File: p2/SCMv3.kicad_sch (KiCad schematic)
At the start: 122 parts, among them IC1 40106, IC2 40106, IC3 TL082, J1 ISP, J1-OUT8 JACK-MONO-SWB, J2 Conn_01x02, J2-OUT7 JACK-MONO-SWB, J3 POWER, J3-OUT6 JACK-MONO-SWB, J4-OUT5 JACK-MONO-SWB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

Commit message: SCM v3 updates
*added missing trace for buttons
*moved trip pot
*flipped pots around
*removed C18 and 21
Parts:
- removed C18, C21: 0.1uF_0603_16V, 4ms_Capacitor:C_0603, symbol 4ms_Capacitor:0.1uF_0603_16V
- D10, D11: JLCPCB ID (none) -> C15759
- IC1, IC2: JLCPCB ID (none) -> C58834
- IC3: JLCPCB ID (none) -> C2652280
- Q1, Q2, Q3, Q4: footprint Package_TO_SOT_SMD:SOT-23 -> 4ms_Package_SOT:SOT23-3_PO132; Display (none) -> Si2318; JLCPCB ID (none) -> C14498
- U1: value ATmega328-A -> ATMEGA328-AU; Alt JLCPCB ID (none) -> C618731; JLCPCB ID (none) -> C14877
- VR1: Alt JLCPCB ID (none) -> C55509; JLCPCB ID (none) -> C58069
- VR2: Alt JLCPCB ID (none) -> C8614; JLCPCB ID (none) -> C122847
- Y1: JLCPCB ID (none) -> C90906
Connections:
- net GND: now also IC1.7 (VSS), IC2.7 (VSS)
- net at BMUTE1.5 (POLE-B), R18.2: now also BMUTE1.2 (POLE-A), R22.2
- net at BFAST1.2 (POLE-A), R7.2: now also BFAST1.5 (POLE-B), R5.2

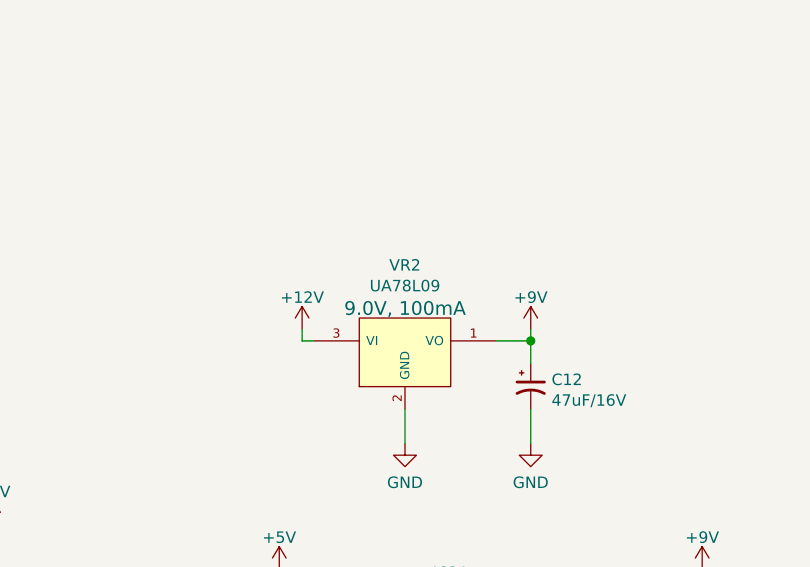
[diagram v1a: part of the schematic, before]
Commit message: replaced 9v reg with 8v reg
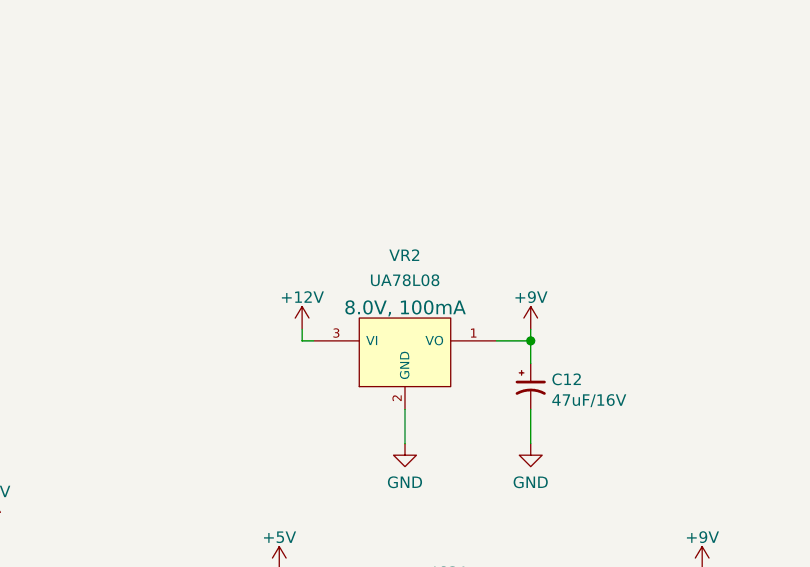
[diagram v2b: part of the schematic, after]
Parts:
- removed VR2: UA78L09, 4ms_Package_SOT:SOT89-3, symbol 4ms_Regulator:UA78L09
- added VR2: UA78L08, 4ms_Package_SOT:SOT89-3, symbol 4ms_Regulator:UA78L08
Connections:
- net +12V: now also VR2.3 (VI)
- net +9V: now also VR2.1 (VO)
- net GND: now also VR2.2 (GND)
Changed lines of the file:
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@@
     (pin "3")
   )
-  (symbol (lib_id "4ms_Regulator:UA78L09") (at 193.04 304.8 0) (unit 1)
+  (symbol (lib_id "4ms_Regulator:UA78L08") (at 193.04 304.8 0) (unit 1)
     (in_bom yes) (on_board yes) (fields_autoplaced)
-    (property "Reference" "VR2" (id 0) (at 193.04 295.1316 0))
-    (property "Value" "UA78L09" (id 1) (at 193.04 297.4303 0))
+    (property "Reference" "VR2" (id 0) (at 193.04 294.0628 0))
+    (property "Value" "UA78L08" (id 1) (at 193.04 296.8379 0))
     (property "Footprint" "4ms_Package_SOT:SOT89-3" (id 2) (at 204.47 317.5 0)
       (effects (font (size 1.27 1.27)) hide)
     )
-    (property "Datasheet" "https://www.ti.com/general/docs/suppproductinfo.tsp?distId=26&gotoUrl=http%3A%2F%2Fwww.ti.com%2Flit%2Fgpn%2Fua78l" (id 3) (at 193.04 304.8 0)
-      (effects (font (size 1.27 1.27)) hide)
-    )
-    (property "Specifications" "Vreg 9.0V, Iout>100mA, Vin>11.5V" (id 4) (at 190.5 312.674 0)
+    (property "Datasheet" "https://www.ti.com/lit/ds/symlink/ua78l.pdf?HQS=dis-mous-null-mousermode-dsf-pf-null-wwe&ts=1629320595639" (id 3) (at 193.04 304.8 0)
+      (effects (font (size 1.27 1.27)) hide)
+    )
+    (property "Specifications" "Vreg 8.0V, Iout>100mA, Vin>10.5V" (id 4) (at 190.5 312.674 0)
       (effects (font (size 1.27 1.27)) (justify left) hide)
     )
@@
       (effects (font (size 1.27 1.27)) (justify left) hide)
     )
-    (property "Part Number" "UA78L09ACPK" (id 6) (at 190.5 315.722 0)
-      (effects (font (size 1.27 1.27)) (justify left) hide)
-    )
-    (property "Display" "9.0V, 100mA" (id 7) (at 193.04 299.9335 0)
+    (property "Part Number" "UA78L08ACPK" (id 6) (at 190.5 315.722 0)
+      (effects (font (size 1.27 1.27)) (justify left) hide)
+    )
+    (property "Display" "8.0V, 100mA" (id 7) (at 193.04 299.865 0)
       (effects (font (size 1.524 1.524)))
-    )
-    (property "JLCPCB ID" "C122847" (id 8) (at 193.04 304.8 0)
-      (effects (font (size 1.27 1.27)) hide)
-    )
-    (property "Alt JLCPCB ID" "C8614" (id 9) (at 193.04 304.8 0)
-      (effects (font (size 1.27 1.27)) hide)
     )
     (pin "1")
@@
       (reference "VR1") (unit 1) (value "L78M05CDT") (footprint "4ms_Package_TO:TO-252-2")
     )
-    (path "/1ca1c557-de06-4822-8b22-57ae4a25cd78"
-      (reference "VR2") (unit 1) (value "UA78L09") (footprint "4ms_Package_SOT:SOT89-3")
+    (path "/d75c3cf8-42d8-4c9a-af69-6743d9e59630"
+      (reference "VR2") (unit 1) (value "UA78L08") (footprint "4ms_Package_SOT:SOT89-3")
     )
     (path "/56d236fd-8965-44b0-8024-00e3f41457df"

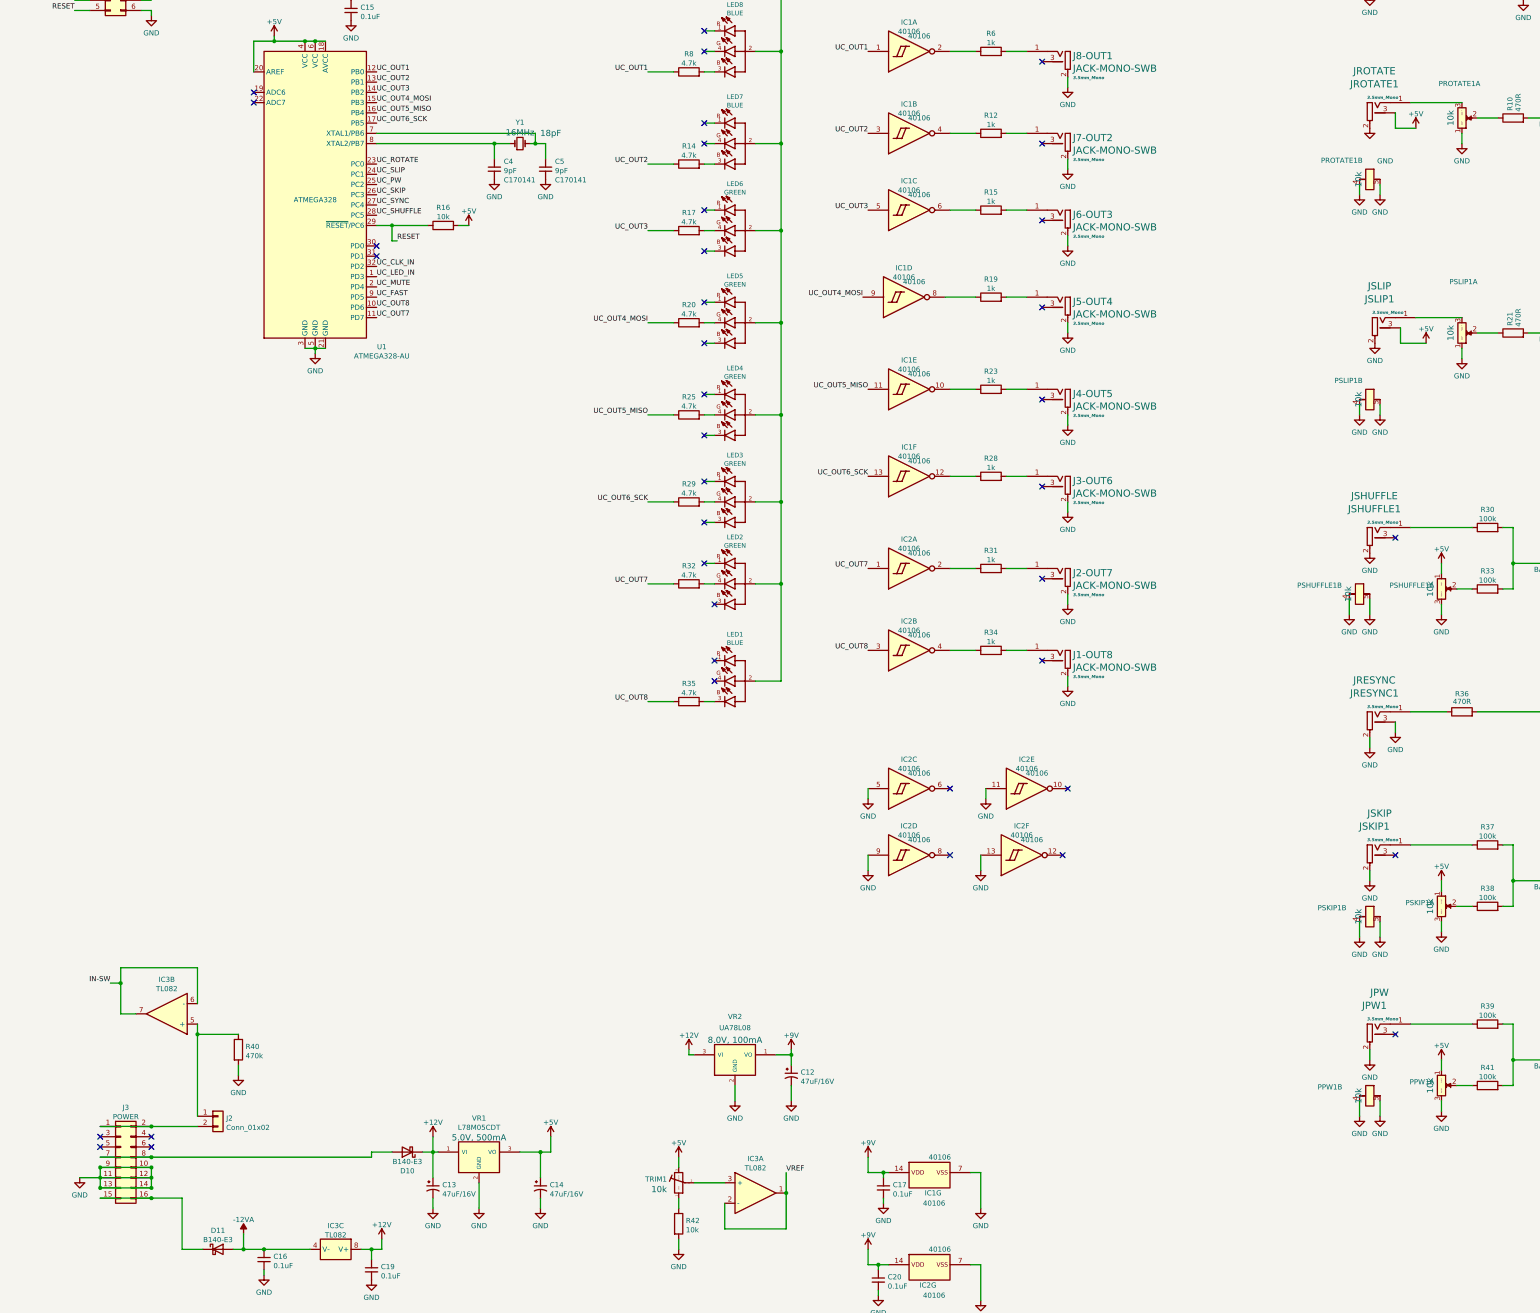
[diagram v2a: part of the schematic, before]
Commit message: added F030 chip (not connected)
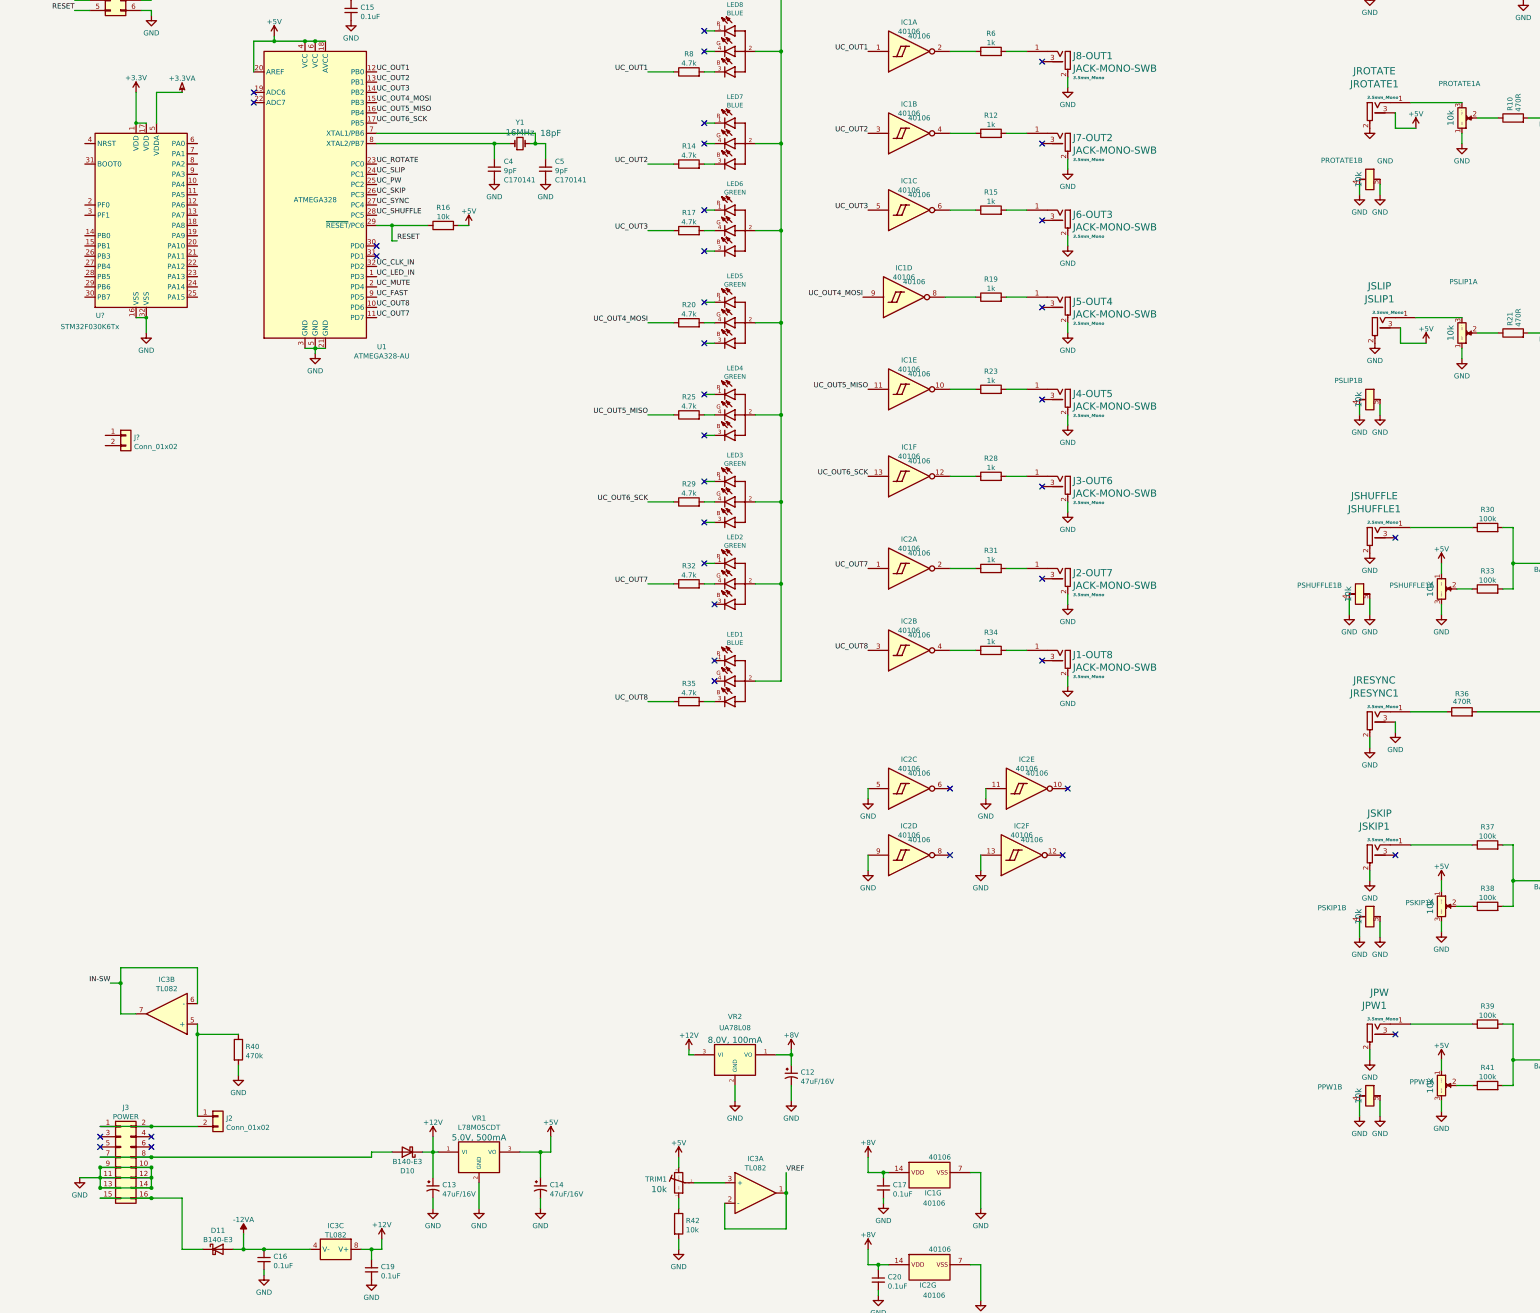
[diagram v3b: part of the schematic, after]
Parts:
- added J?: Conn_01x02, 4ms_Connector:Pins_1x02_2.54mm_TH, symbol 4ms_Connector:Conn_01x02
- added U?: STM32F030K6Tx, Package_QFP:LQFP-32_7x7mm_P0.8mm, symbol MCU_ST_STM32F0:STM32F030K6Tx
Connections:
- net GND: now also U?.16 (VSS), U?.32 (VSS)
- net +9V renamed +8V
- new net +3.3VA: U?.5 (VDDA)
- new net +3V3: U?.1 (VDD), U?.17 (VDD)
